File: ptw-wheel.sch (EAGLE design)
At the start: 5 parts

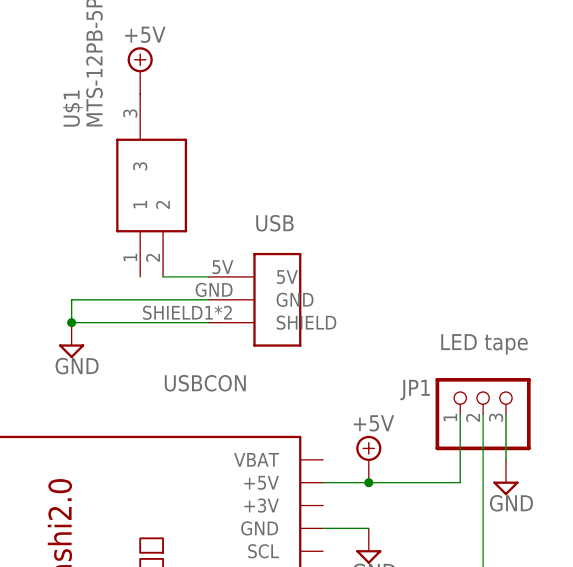
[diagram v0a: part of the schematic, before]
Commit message: - Write down module names - Modify layout
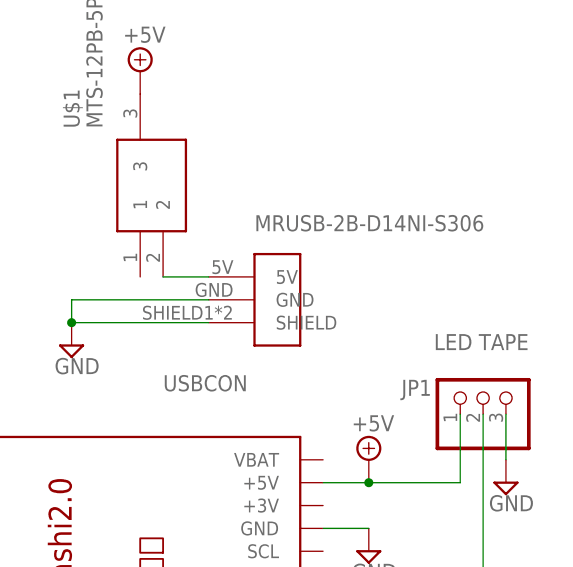
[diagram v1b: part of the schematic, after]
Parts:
- JP1: value LED tape -> LED TAPE
- renumbered USB to MRUSB-2B-D14NI-S306
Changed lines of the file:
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@@
 </classes>
 <parts>
-<part name="JP1" library="pinhead" library_urn="urn:adsk.eagle:library:325" deviceset="PINHD-1X3" device="" package3d_urn="urn:adsk.eagle:package:22458/2" value="LED tape"/>
-<part name="USB" library="usbcon" deviceset="USBCON" device=""/>
+<part name="JP1" library="pinhead" library_urn="urn:adsk.eagle:library:325" deviceset="PINHD-1X3" device="" package3d_urn="urn:adsk.eagle:package:22458/2" value="LED TAPE"/>
+<part name="MRUSB-2B-D14NI-S306" library="usbcon" deviceset="USBCON" device=""/>
 <part name="ARDUINO_NANO" library="ArduinoNanoV30" deviceset="ARDUINO_NANO" device=""/>
 <part name="SUPPLY1" library="supply2" library_urn="urn:adsk.eagle:library:372" deviceset="GND" device=""/>
@@
 <attribute name="VALUE" x="129.54" y="57.15" size="1.778" layer="96" rot="R180"/>
 </instance>
-<instance part="USB" gate="G$1" x="93.98" y="60.96" smashed="yes">
+<instance part="MRUSB-2B-D14NI-S306" gate="G$1" x="93.98" y="60.96" smashed="yes">
 <attribute name="NAME" x="99.06" y="68.58" size="1.778" layer="95"/>
 <attribute name="VALUE" x="88.9" y="50.8" size="1.778" layer="96"/>
@@
 <net name="GND" class="0">
 <segment>
-<pinref part="USB" gate="G$1" pin="GND"/>
+<pinref part="MRUSB-2B-D14NI-S306" gate="G$1" pin="GND"/>
 <wire x1="93.98" y1="60.96" x2="78.74" y2="60.96" width="0.1524" layer="91"/>
 <wire x1="78.74" y1="60.96" x2="78.74" y2="58.42" width="0.1524" layer="91"/>
-<pinref part="USB" gate="G$1" pin="SHIELD"/>
+<pinref part="MRUSB-2B-D14NI-S306" gate="G$1" pin="SHIELD"/>
 <wire x1="93.98" y1="58.42" x2="78.74" y2="58.42" width="0.1524" layer="91"/>
 <junction x="78.74" y="58.42"/>
@@
 <net name="N$1" class="0">
 <segment>
-<pinref part="USB" gate="G$1" pin="5V"/>
+<pinref part="MRUSB-2B-D14NI-S306" gate="G$1" pin="5V"/>
 <wire x1="93.98" y1="63.5" x2="88.9" y2="63.5" width="0.1524" layer="91"/>
 <pinref part="U$1" gate="G$1" pin="2"/>
